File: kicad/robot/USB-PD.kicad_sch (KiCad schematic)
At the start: 34 parts, among them U11 MAX77958EWV+T

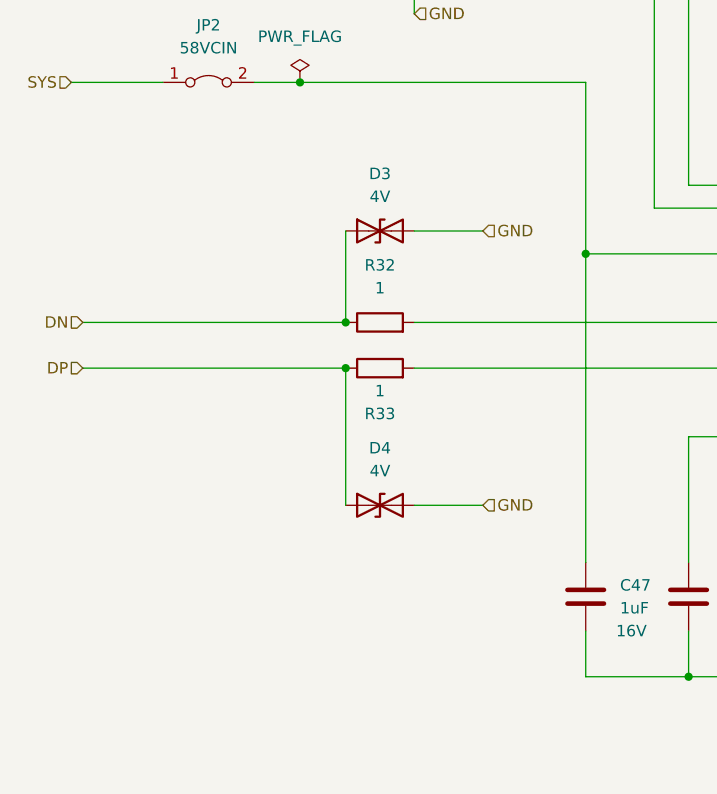
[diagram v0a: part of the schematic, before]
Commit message: replaced TVS diodes on DP/DN lines
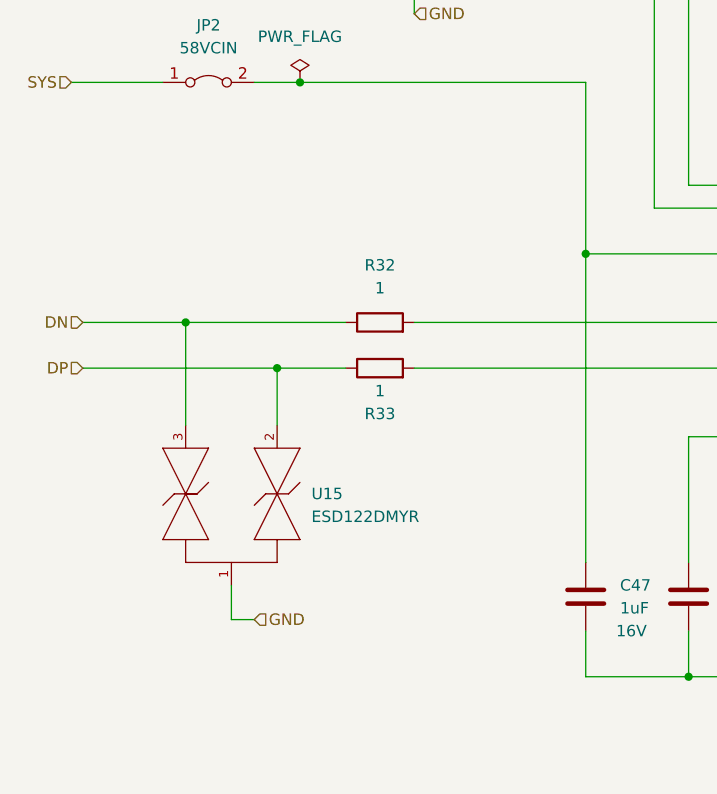
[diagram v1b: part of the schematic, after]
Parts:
- removed D3, D4: 4V, symbol Device:D_TVS
- added U15: ESD122DMYR, Diode_SMD:Texas_Instruments-DMY0003A-0-0-MFG, symbol Diode:ESD122DMYR
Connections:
- net DN: now also U15.3 (IO2)
- net DP: now also U15.2 (IO1)
- net GND: now also U15.1 (GND)
